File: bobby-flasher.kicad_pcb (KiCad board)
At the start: 2 copper layers, 19.5 x 36 mm, 20 parts, among them J1 Conn_01x03, J2 Conn_01x06, J3 Flash, Q1 SS8050_C2150, Q2 SS8050_C2150, U1 CH343G, U2 AMS1117-3.3

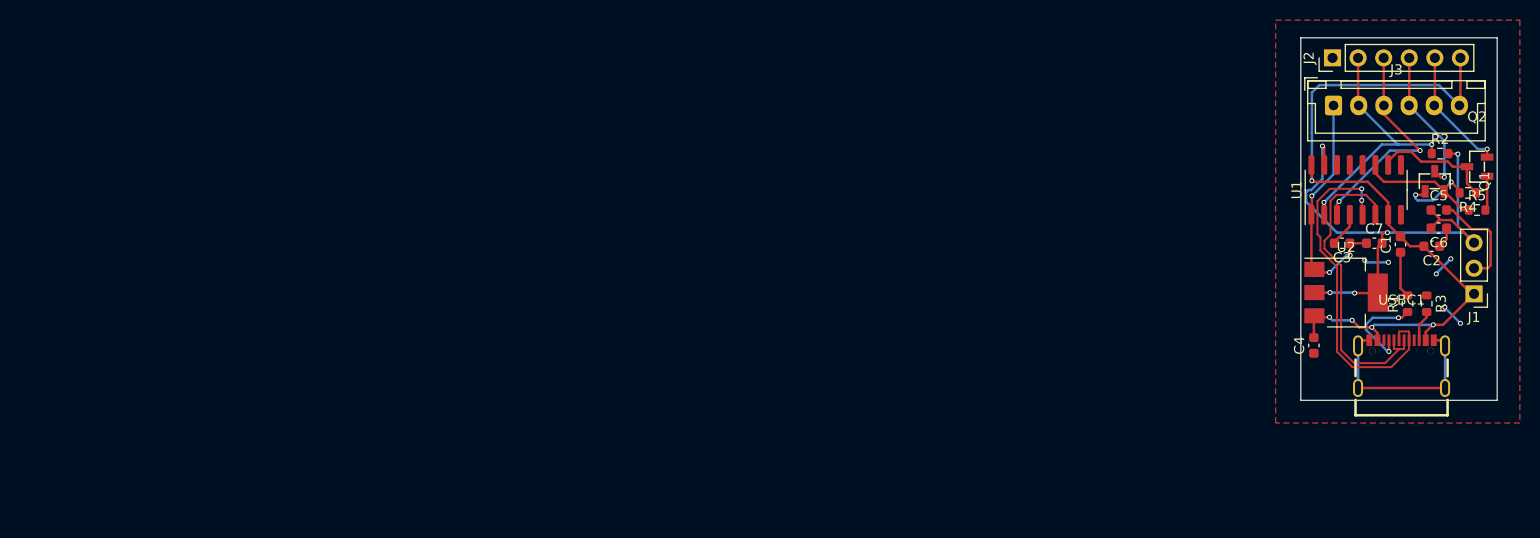
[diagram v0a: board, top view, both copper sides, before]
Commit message: new layout, added leds
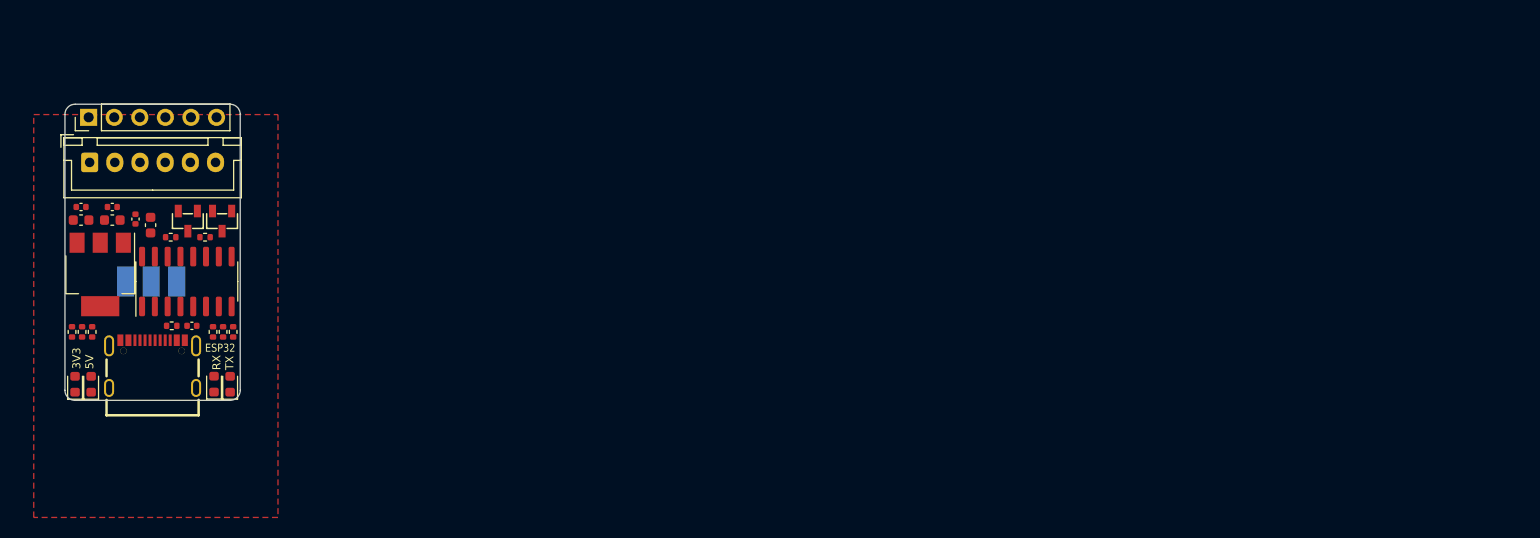
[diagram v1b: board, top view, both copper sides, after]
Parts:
- added D1: LED, LED_SMD:LED_0603_1608Metric, F.Cu at (-6.10, 79.4)
- added D2: LED, LED_SMD:LED_0603_1608Metric, F.Cu at (-7.70, 79.4)
- added D3: LED, LED_SMD:LED_0603_1608Metric, F.Cu at (6.10, 79.4)
- added D4: LED, LED_SMD:LED_0603_1608Metric, F.Cu at (7.70, 79.4)
- added R6: 1k, Resistor_SMD:R_0402_1005Metric, F.Cu at (-7.00, 74.2)
- added R7: 1k, Resistor_SMD:R_0402_1005Metric, F.Cu at (-8.00, 74.2)
- added R8: 1k, Resistor_SMD:R_0402_1005Metric, F.Cu at (6.00, 74.2)
- added R9: 1k, Resistor_SMD:R_0402_1005Metric, F.Cu at (8.00, 74.2)
- C1, C3, C4, C6: footprint Capacitor_SMD:C_0603_1608Metric -> Capacitor_SMD:C_0402_1005Metric
- J1: moved to B.Cu
- R1, R2, R3, R4, R5: footprint Resistor_SMD:R_0603_1608Metric -> Resistor_SMD:R_0402_1005Metric
- moved C2 134.1 mm to (-7.10, 63.1), turned to 0 degrees
- moved C6 131.7 mm to (-4.00, 61.8)
- moved C5 131.7 mm to (-4.00, 63.1)
- moved C1 131.1 mm to (-7.10, 61.8), turned to 0 degrees
- moved R1 130.6 mm to (-6.00, 74.2), turned to -90 degrees
- moved R4 128.9 mm to (1.80, 64.8), turned to 0 degrees
- moved J1 128.8 mm to (2.40, 69.2), turned to 90 degrees
- moved R5 126.3 mm to (5.21, 64.8), turned to 180 degrees
- moved Q2 124.7 mm to (6.90, 63.2), turned to 90 degrees
- moved R3 124.6 mm to (1.90, 73.6), turned to 180 degrees
- moved USBC1 124.0 mm to (0.00, 77.4)
- moved Q1 123.9 mm to (3.50, 63.2), turned to 90 degrees
- moved U2 123.7 mm to (-5.20, 68.5), turned to -90 degrees
- moved J2 123.6 mm to (-6.35, 52.9)
- moved J3 123.6 mm to (-6.25, 57.4)
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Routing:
- net +5V: track 76.2 -> 0.00 mm, vias 5 -> 0
- net GND: track 68.0 -> 0.00 mm, vias 9 -> 0
- net +3V3: track 55.5 -> 0.00 mm, vias 5 -> 0
- net USB_DP: track 35.4 -> 0.00 mm, vias 2 -> 0
- net USB_DN: track 31.4 -> 0.00 mm
- net ESP_RX: track 25.6 -> 0.00 mm, vias 2 -> 0
- net ESP_TX: track 22.3 -> 0.00 mm, vias 2 -> 0
- net EN: track 14.5 -> 0.00 mm, vias 1 -> 0
- net IO0: track 12.6 -> 0.00 mm, vias 1 -> 0
- net DTR: track 12.2 -> 0.00 mm
- net RTS: track 11.6 -> 0.00 mm
- net Net-(R1-Pad1): track 9.62 -> 0.00 mm, vias 2 -> 0
- net Net-(Q1-Pad1): track 7.24 -> 0.00 mm, vias 2 -> 0
- net Net-(C3-Pad2): track 3.46 -> 0.00 mm
- net Net-(Q2-Pad1): track 3.42 -> 0.00 mm
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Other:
- board size 19.5 x 36 mm -> 17.4 x 29.4 mm
- board text added: "3V3 5V"
- board text added: "5V GND 3V3"
- board text added: "5V IO0 EN TX RX GND"
- board text added: "ESP32"
- board text added: "RX TX"

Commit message: Updated pcb
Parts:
- moved C3 0.25 mm to (3.65, 73.6)
- moved R3 0.15 mm to (1.75, 73.6)
- turned R6 to -90 degrees
- turned R7 to -90 degrees
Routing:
- net +5V: track 0.00 -> 73.5 mm, vias 0 -> 6
- net +3V3: track 0.00 -> 47.2 mm, vias 0 -> 3
- net ESP_TX: track 0.00 -> 44.3 mm, vias 0 -> 3
- net ESP_RX: track 0.00 -> 41.0 mm, vias 0 -> 4
- net GND: track 0.00 -> 21.8 mm, vias 0 -> 28
- net DTR: track 0.00 -> 15.4 mm, vias 0 -> 2
- net USB_DN: track 0.00 -> 14.7 mm
- net EN: track 0.00 -> 12.4 mm, vias 0 -> 1
- net Net-(Q2-Pad1): track 0.00 -> 12.2 mm
- net IO0: track 0.00 -> 10.2 mm
- net USB_DP: track 0.00 -> 8.10 mm
- net RTS: track 0.00 -> 6.98 mm
- net Net-(Q1-Pad1): track 0.00 -> 6.62 mm
- net Net-(R1-Pad1): track 0.00 -> 6.14 mm
- net Net-(C3-Pad2): track 0.00 -> 6.00 mm
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- added copper zone on B.Cu, net GND

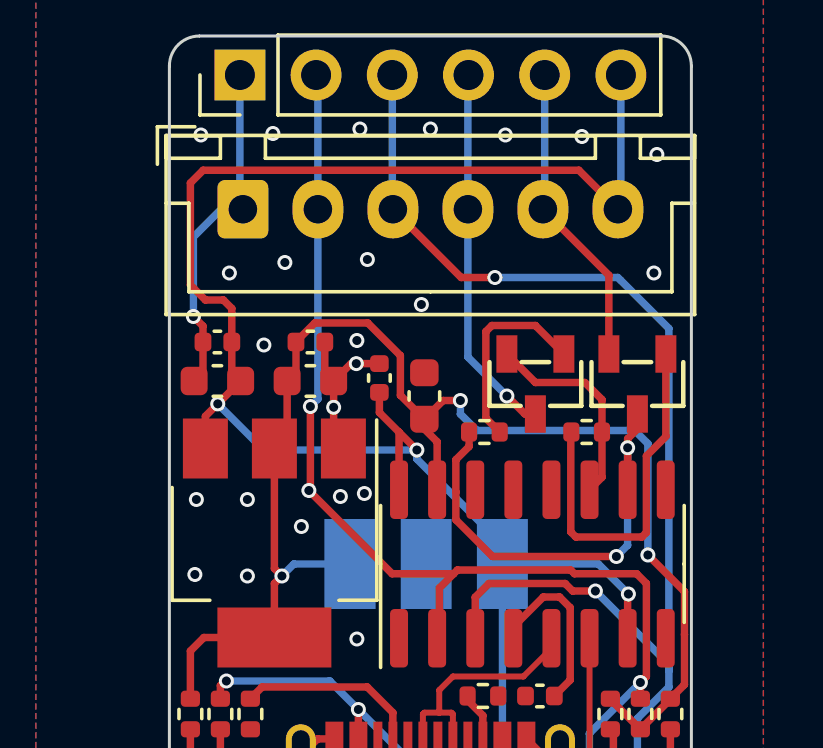
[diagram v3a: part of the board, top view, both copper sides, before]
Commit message: peters fixes, resistor on DTR missing
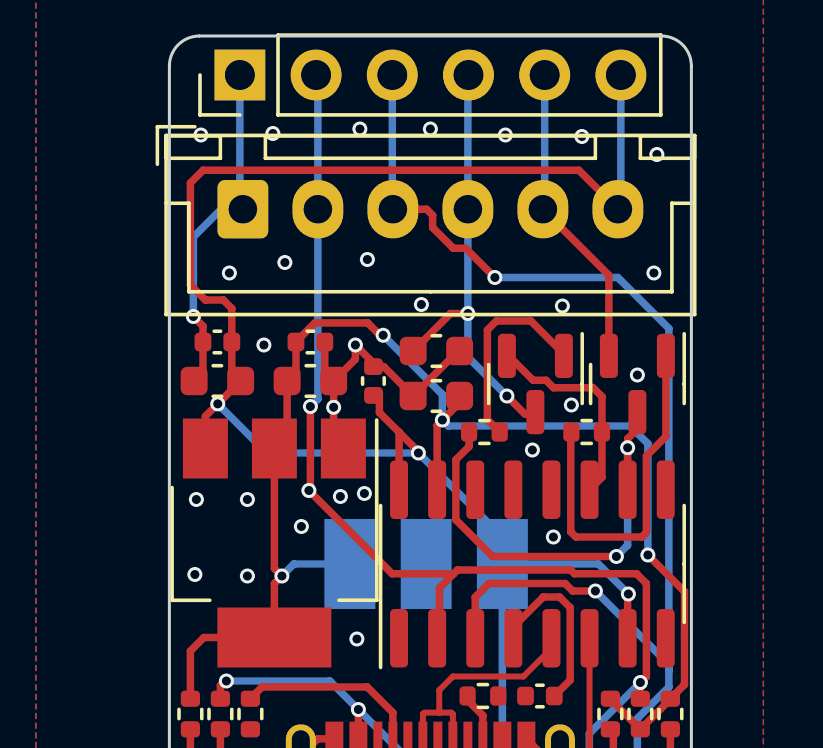
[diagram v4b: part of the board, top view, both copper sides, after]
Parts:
- added C8: 10u, Capacitor_SMD:C_0603_1608Metric, F.Cu at (0.20, 62.1)
- Q1, Q2: footprint SS8050:SOT-23-3_L2.9-W1.3-P1.90-LS2.4-BR -> Package_TO_SOT_SMD:SOT-23
- moved C7 0.40 mm to (0.20, 63.6), turned to 0 degrees
- moved C4 0.22 mm to (-1.90, 63.1)
- turned Q1 to -90 degrees
- turned Q2 to -90 degrees
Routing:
- net GND: track 21.8 -> 26.5 mm, vias 28 -> 32
- net EN: track 12.4 -> 14.8 mm, vias 1 -> 2
- net +3V3: track 47.2 -> 47.0 mm, vias 3 -> 4

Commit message: fixed version
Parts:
- added R10: 10k, Resistor_SMD:R_0402_1005Metric, F.Cu at (-0.10, 64.9)
- moved C4 0.50 mm to (-1.90, 62.6)
- moved R5 0.19 mm to (5.40, 64.8)
- moved R4 0.10 mm to (1.80, 64.9)
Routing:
- net GND: track 26.5 -> 32.1 mm
- net +3V3: track 47.0 -> 51.4 mm
- net DTR: track 15.4 -> 16.4 mm
- net Net-(Q2-Pad1): track 12.2 -> 11.6 mm
- net +5V: track 73.6 -> 73.7 mm, vias 6 -> 7
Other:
- board text added: "5V IO0 EN RX TX TX RX GND"
- board text added: "ESP32 Flasher"
- board text removed: "5V IO0 EN TX RX GND"
